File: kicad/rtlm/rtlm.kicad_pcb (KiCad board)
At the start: 2 copper layers, 262 parts, among them IC1 ESP32-S3FN8, IC2 TPS25940ARVCR, IC3 PE4259, IC4 TPS2553DBVR, IC5 TLV9004IDR, IC6 TLV9004IDR, IC7 TCAN1042HGVDR, IC8 TPS2553DBVR, IC9 TLC59116IPWR, J1 USB_C_Receptacle_USB2.0_16P, J10 TEMP_2, J11 TEMP_3, J12 TEMP_4, J13 ANALOG_1, J14 ANALOG_2, J15 ANALOG_3, J16 ANALOG_4, J17 DM3AT-SF-PEJM5, J18 CAN_EXPANSION, J19 BATTERY_IN, J2 Conn_01x02, J20 BATTERY_OUT, J3 UART_DEBUG_3V3, J4 LORA_ANT, J5 PULSE_1, J6 PULSE_2, J7 PULSE_3, J8 PULSE_4, J9 TEMP_1, Q1 DMP2035U-7, SW1 SW_Push, SW2 SW_Push, U1 TPS62130A, U10 RV-3028-C7, U2 TPS2116DRL, U3 TPD2EUSB30, U4 SX1262IMLTRT, U5 SN74LVC14ADR, U6 MCP3208-BI/SL, U7 REF3025AIDBZR, U8 AMC3330, U9 ADS1115IDGS, Y1 40MHz, Y2 TG2520SMN 32.0000M-MCGNNM3

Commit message: feat: prelim PCB layout, no routing
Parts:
- moved R61 270.7 mm to (197.8, 270.4), turned to 90 degrees
- moved C56 260.6 mm to (184.7, 260.8)
- moved C55 258.5 mm to (173.2, 261.5), turned to 180 degrees
- moved C54 257.1 mm to (173.2, 257.5), turned to 180 degrees
- moved C57 256.2 mm to (184.7, 258.3)
- moved R45 255.9 mm to (139.0, 273.8), turned to -90 degrees
- moved D34 255.2 mm to (194.5, 269.8), turned to 90 degrees
- moved R46 253.9 mm to (141.0, 273.8), turned to 90 degrees
- moved D33 253.7 mm to (183.2, 269.8), turned to 90 degrees
- moved D32 252.7 mm to (171.8, 269.8), turned to 90 degrees
- moved R63 252.6 mm to (174.0, 265.8), turned to 90 degrees
- moved D31 252.3 mm to (160.8, 269.8), turned to 90 degrees
- moved R65 251.7 mm to (184.0, 265.8), turned to 90 degrees
- moved D20 251.6 mm to (46.8, 275.0), turned to 90 degrees
- moved D25 251.4 mm to (69.8, 275.0), turned to 90 degrees
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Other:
- board text added: "BOOT"
- board text added: "FLT"
- board text added: "LOG"
- board text added: "PWR"
- board text added: "RAD"
- board text added: "RESET"

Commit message: chore: update history
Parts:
- moved BT1 298.1 mm to (426.2, 189.0)
- moved C1 298.1 mm to (344.1, 210.0)
- moved C10 298.1 mm to (376.7, 205.5)
- moved C11 298.1 mm to (389.2, 208.5)
- moved C12 298.1 mm to (380.0, 213.2)
- moved C13 298.1 mm to (382.0, 213.2)
- moved C14 298.1 mm to (389.7, 204.0)
- moved C15 298.1 mm to (389.7, 202.5)
- moved C16 298.1 mm to (394.1, 202.0)
- moved C17 298.1 mm to (385.5, 200.7)
- moved C18 298.1 mm to (383.5, 200.7)
- moved C19 298.1 mm to (395.8, 207.5)
- moved C2 298.1 mm to (344.1, 207.0)
- moved C20 298.1 mm to (392.8, 204.5)
- moved C21 298.1 mm to (342.2, 166.8)
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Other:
- board outline added: 225 x 140 mm
- copper layers 2 -> 4

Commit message: feat: remove battery passthrough, start routing
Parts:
- removed J20: BATTERY_OUT, Connector_AMASS:AMASS_XT60PW-M_1x02_P7.20mm_Horizontal
- added H1: MountingHole_3.2mm_M3, MountingHole:MountingHole_3.2mm_M3, F.Cu at (199.5, 170.0)
- added H2: MountingHole_3.2mm_M3, MountingHole:MountingHole_3.2mm_M3, F.Cu at (389.5, 170.0)
- added H3: MountingHole_3.2mm_M3, MountingHole:MountingHole_3.2mm_M3, F.Cu at (199.5, 270.0)
- added H4: MountingHole_3.2mm_M3, MountingHole:MountingHole_3.2mm_M3, F.Cu at (389.5, 270.0)
- J19: value BATTERY_IN -> BATTERY_VOLTAGE_SENSE_LINE; footprint Connector_AMASS:AMASS_XT60PW-F_1x02_P7.20mm_Horizontal -> Connector_Molex:Molex_Micro-Fit_3.0_43650-0300_1x03_P3.00mm_Horizontal
- moved J19 137.4 mm to (348.2, 174.5)
- moved J4 129.8 mm to (220.8, 174.2), turned to 180 degrees
- moved C7 128.3 mm to (217.2, 188.1)
- moved C8 128.3 mm to (220.0, 196.6)
- moved C9 128.3 mm to (214.8, 196.6)
- moved IC2 128.3 mm to (217.8, 192.3)
- moved R11 128.3 mm to (220.4, 187.8)
- moved R12 128.3 mm to (221.6, 191.3)
- moved R13 128.3 mm to (221.6, 189.6)
- moved R14 128.3 mm to (222.4, 193.1)
- moved R15 128.3 mm to (222.4, 194.8)
- moved C30 127.2 mm to (224.1, 172.4), turned to 90 degrees
- moved Q1 126.2 mm to (209.8, 190.0), turned to 180 degrees
- moved C31 125.8 mm to (225.3, 172.4), turned to 90 degrees
- moved L6 125.3 mm to (224.6, 174.2), turned to 0 degrees
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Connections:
- J19 pad 2: /PACK_POS -> unconnected-(J19-Pin_2-Pad2)
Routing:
- net /EXT_5V_POLARITY_OK: track 0.00 -> 25.7 mm, vias 0 -> 2
- net /EXT_5V_RAW: track 0.00 -> 8.83 mm
- net Net-(D1-A): track 0.00 -> 6.32 mm
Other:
- board size 225 x 140 mm -> 200 x 110 mm

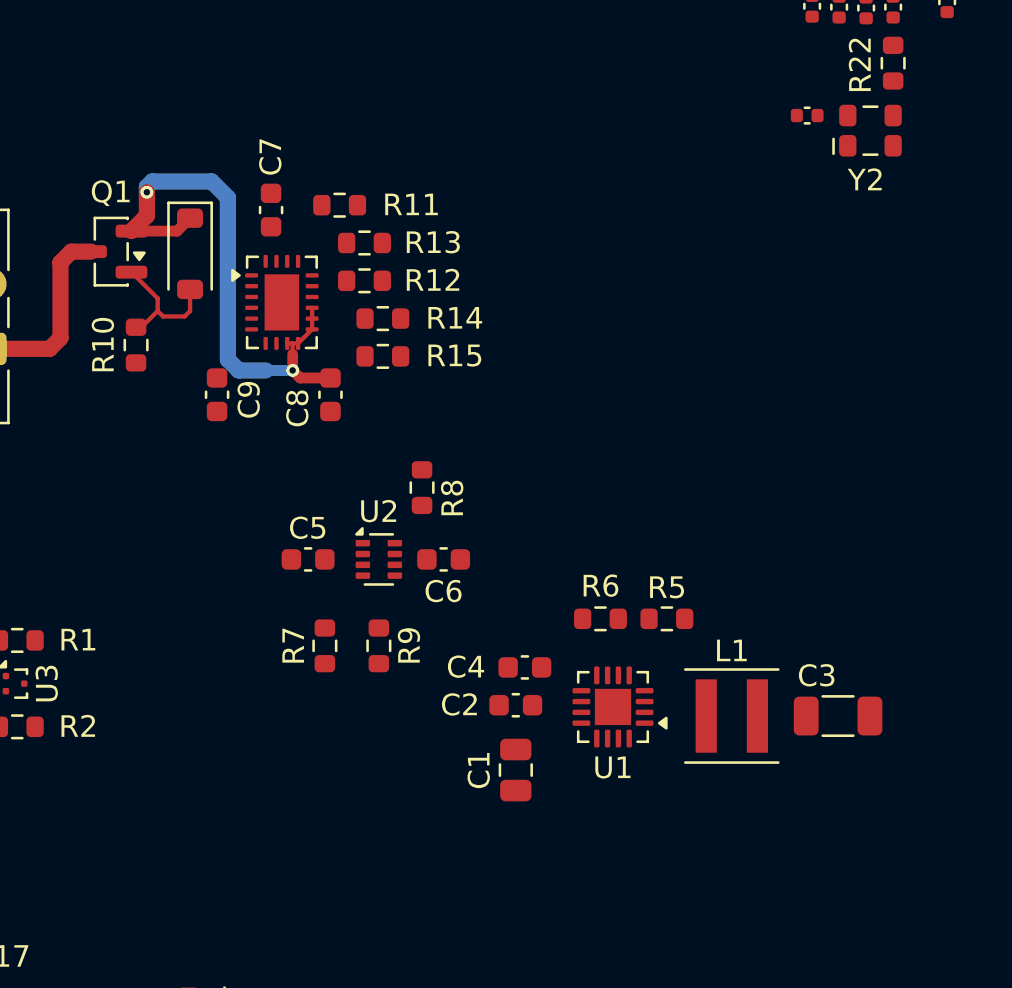
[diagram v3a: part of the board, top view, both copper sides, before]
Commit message: feat: start routing power input
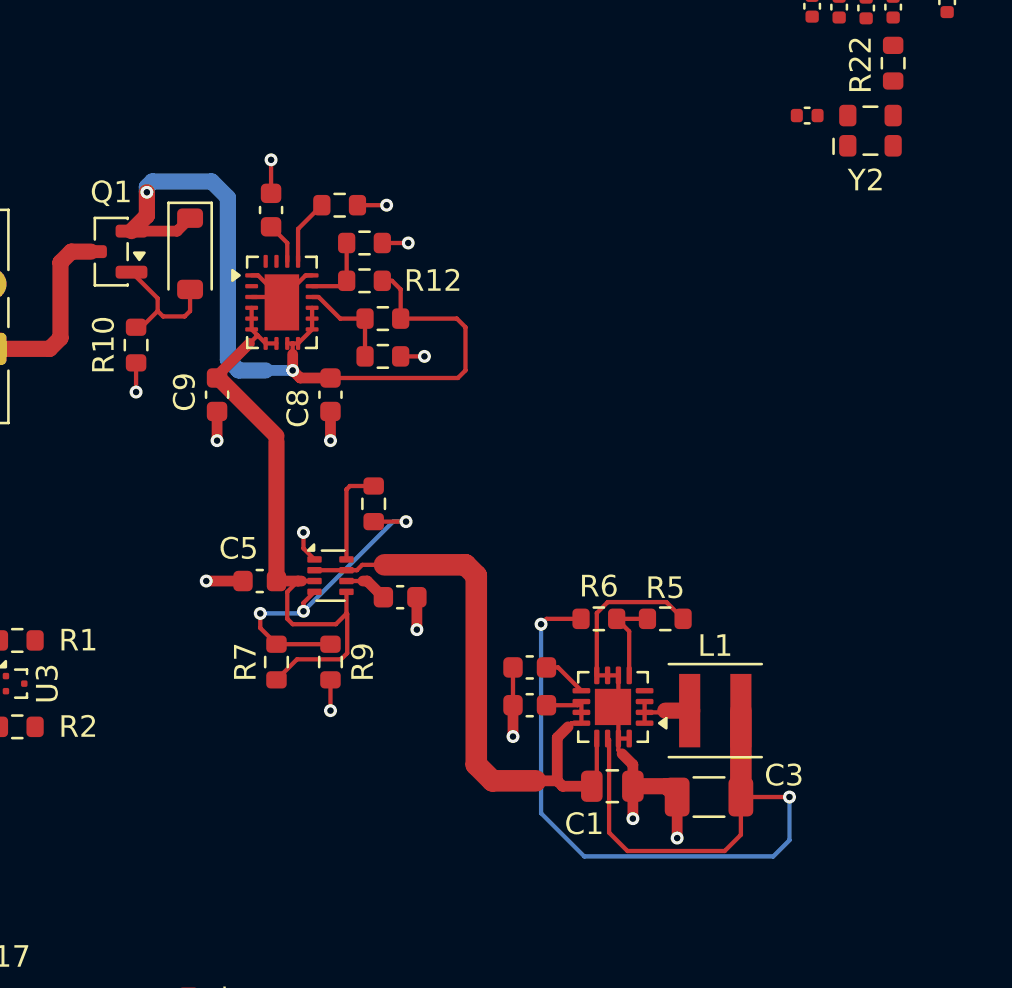
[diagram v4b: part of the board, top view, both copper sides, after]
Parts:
- moved C3 7.05 mm to (237.5, 215.2), turned to 180 degrees
- moved C1 4.53 mm to (233.1, 214.8), turned to 180 degrees
- moved C6 2.67 mm to (223.2, 206.0)
- moved C5 2.45 mm to (216.7, 205.2)
- moved R7 2.36 mm to (217.5, 209.0)
- moved R8 2.36 mm to (222.0, 201.7)
- moved R9 2.36 mm to (220.0, 209.0)
- moved U2 2.36 mm to (220.0, 205.0)
- moved L1 0.80 mm to (237.8, 211.2)
- moved C2 0.64 mm to (229.2, 211.0)
- moved C4 0.22 mm to (229.2, 209.2)
- moved R5 0.07 mm to (235.5, 207.0)
- moved R6 0.07 mm to (232.4, 207.0)
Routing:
- net +3.3V: track 0.00 -> 44.5 mm, vias 0 -> 2
- net GND: track 0.00 -> 44.1 mm, vias 0 -> 14
- net /5V_SYS: track 0.00 -> 30.7 mm
- net /EXT_5V_PROTECTED: track 0.00 -> 28.8 mm
- net /PWR_PRIORITY: track 0.00 -> 15.4 mm, vias 0 -> 3
- net /EXT_5V_POLARITY_OK: track 25.7 -> 39.7 mm
- net Net-(IC2-EN): track 0.00 -> 4.61 mm
- net Net-(U2-ST): track 0.00 -> 4.57 mm
- net Net-(U1-FB): track 0.00 -> 4.28 mm
- net Net-(IC2-OVP): track 0.00 -> 3.45 mm
- net Net-(L1-Pad1): track 0.00 -> 3.24 mm
- net Net-(IC2-ILIM): track 0.00 -> 3.06 mm
- net Net-(U1-SS/TR): track 0.00 -> 2.29 mm
- net /USB_5V: track 0.00 -> 2.02 mm
- net Net-(IC2-DVDT): track 0.00 -> 1.91 mm

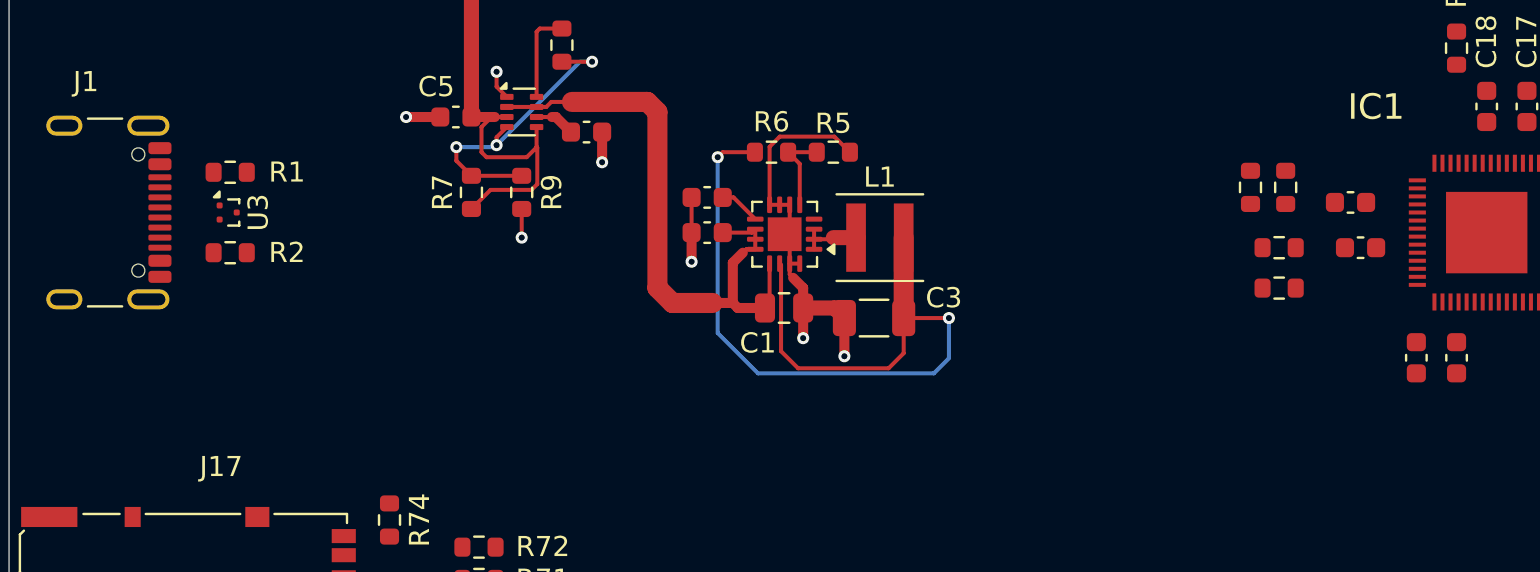
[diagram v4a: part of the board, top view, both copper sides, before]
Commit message: feat: USB routing, thermal vias
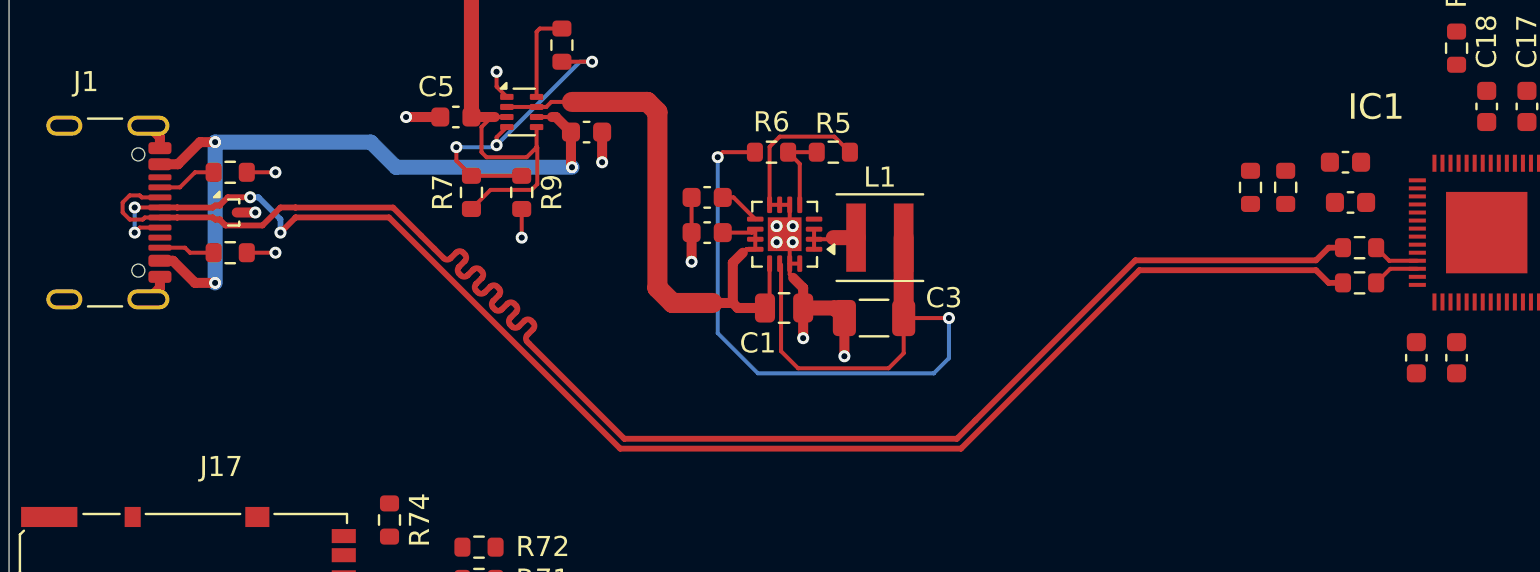
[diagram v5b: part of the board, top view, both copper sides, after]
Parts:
- moved C59 4.32 mm to (261.0, 207.5)
- moved R4 4.01 mm to (261.7, 213.5)
- moved R3 4.00 mm to (261.7, 211.8)
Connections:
- net /USB_DM renamed /USB_DN
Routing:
- net /USB_DN: track 0.00 -> 79.2 mm
- net /USB_DP: track 0.00 -> 73.1 mm, vias 0 -> 4
- net /USB_5V: track 2.02 -> 35.5 mm, vias 0 -> 3
- net GND: track 44.1 -> 50.6 mm, vias 14 -> 21
- net Net-(J1-CC1): track 0.00 -> 2.98 mm
- net Net-(J1-CC2): track 0.00 -> 2.77 mm
- net Net-(IC1-GPIO20): track 0.00 -> 2.34 mm
- net Net-(IC1-GPIO19): track 0.00 -> 2.32 mm
- added copper zone on In1.Cu, net GND
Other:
- board text added: "U1 thermal vias: 0.30 mm finished holes, 0.60 mm pads. Tent bottom side; no bottom solder-mask openings."

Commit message: feat: more thermal vias, start power routing
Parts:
- moved C13 0.91 mm to (267.4, 217.2)
- moved C12 0.90 mm to (265.4, 217.2)
- moved C10 0.82 mm to (261.7, 210.2)
- moved C20 0.25 mm to (277.3, 208.2)
- moved C14 0.06 mm to (274.2, 208.1)
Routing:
- net +3.3V: track 44.5 -> 57.1 mm
- net GND: track 50.6 -> 56.3 mm, vias 21 -> 31
- net /ESP_VDD_SPI: track 0.00 -> 4.00 mm
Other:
- board text added: "U1/IC2 thermal vias: 0.30 mm finished holes, 0.60 mm pads. Tent bottom side; no bottom solder-mask openings."
- board text removed: "U1 thermal vias: 0.30 mm finished holes, 0.60 mm pads. Tent bottom side; no bottom solder-mask openings."

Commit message: Add files via upload
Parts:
- moved R13 5.06 mm to (224.2, 193.9), turned to -90 degrees
- moved R12 4.98 mm to (225.8, 193.9), turned to 90 degrees
- moved R10 4.78 mm to (212.0, 199.0)
- moved Q1 4.72 mm to (208.4, 194.5)
- moved D1 4.65 mm to (212.0, 194.5)
- moved R7 3.44 mm to (220.7, 207.8), turned to -90 degrees
- moved R11 1.56 mm to (219.0, 188.5), turned to -90 degrees
- moved R14 1.51 mm to (221.2, 193.9), turned to -90 degrees
- moved R9 1.45 mm to (219.2, 207.8)
- moved C9 1.40 mm to (214.2, 195.3)
- moved R8 1.19 mm to (221.6, 202.8), turned to 0 degrees
- moved C8 1.14 mm to (218.9, 196.4), turned to 180 degrees
- moved R15 0.96 mm to (222.7, 193.9), turned to -90 degrees
- moved IC2 0.90 mm to (217.8, 193.2)
- moved R6 0.59 mm to (231.9, 207.3)
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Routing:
- net /EXT_5V_POLARITY_OK: track 39.7 -> 23.6 mm
- net /EXT_5V_PROTECTED: track 28.8 -> 22.6 mm
- net +3.3V: track 57.1 -> 51.4 mm
- net /EXT_5V_RAW: track 8.83 -> 3.50 mm
- net Net-(IC2-OVP): track 3.45 -> 7.31 mm
- net Net-(U2-ST): track 4.57 -> 1.47 mm
- net GND: track 56.3 -> 54.0 mm, vias 31 -> 32
- net Net-(D1-A): track 6.32 -> 4.94 mm
- net Net-(IC2-EN): track 4.61 -> 3.52 mm
- net Net-(IC2-ILIM): track 3.06 -> 2.27 mm

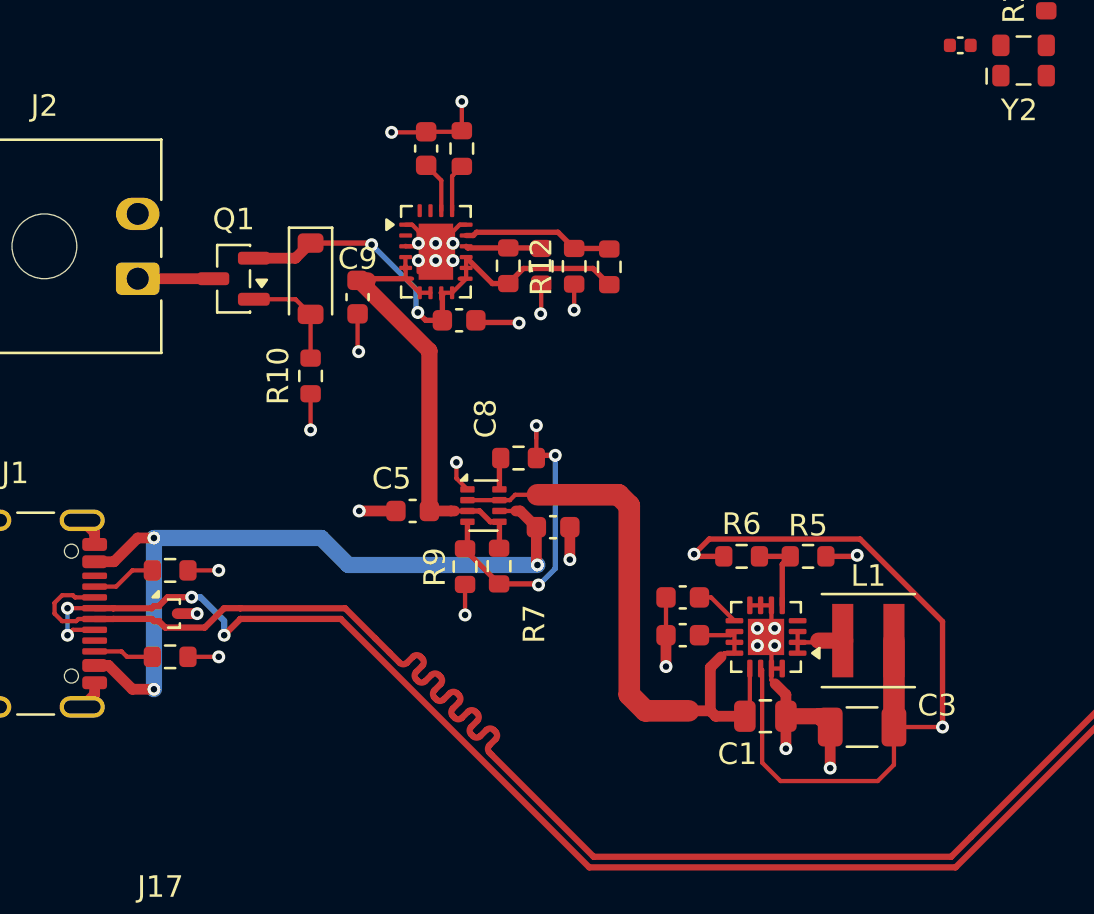
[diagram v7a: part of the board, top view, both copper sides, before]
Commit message: fix: cleanup routing and set uniform trace widths; fix DRC errors
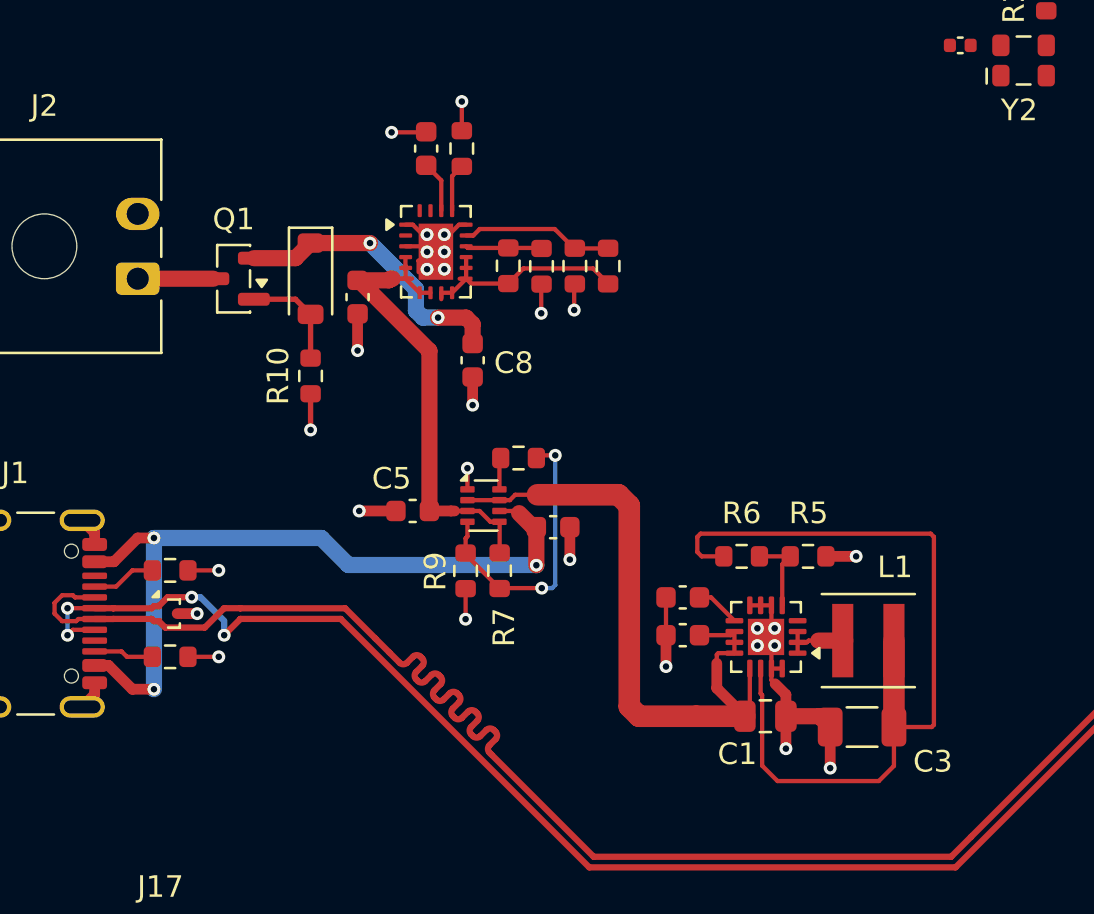
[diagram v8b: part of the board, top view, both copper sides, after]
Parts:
- moved C8 1.95 mm to (219.5, 198.3), turned to 90 degrees
- moved R7 0.22 mm to (220.8, 208.0)
- moved R9 0.20 mm to (219.2, 208.0)
- moved R12 0.07 mm to (225.8, 193.9)
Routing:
- net GND: track 54.0 -> 51.4 mm
- net +3.3V: track 51.4 -> 53.3 mm, vias 2 -> 0
- net /PWR_PRIORITY: track 14.9 -> 13.3 mm, vias 3 -> 2
- net /5V_SYS: track 30.7 -> 31.5 mm
- net /EXT_5V_PROTECTED: track 22.6 -> 22.0 mm
